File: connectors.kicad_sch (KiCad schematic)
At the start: 4 parts, among them J1 Conn_01x04_Pin, J2 Conn_01x04_Pin, J3 Conn_01x09_Pin, J4 Conn_02x03_Odd_Even

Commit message: Completed symbol-footprint associations.
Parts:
- J1, J2: footprint (none) -> Connector_PinHeader_2.54mm:PinHeader_1x04_P2.54mm_Vertical
- J3: footprint (none) -> Connector_PinHeader_2.54mm:PinHeader_1x09_P2.54mm_Vertical
- J4: footprint (none) -> Connector_PinHeader_2.54mm:PinHeader_2x03_P2.54mm_Vertical
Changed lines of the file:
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@@
       (effects (font (size 1.27 1.27)))
     )
-    (property "Footprint" "" (at 134.62 114.3 0)
+    (property "Footprint" "Connector_PinHeader_2.54mm:PinHeader_2x03_P2.54mm_Vertical" (at 134.62 114.3 0)
       (effects (font (size 1.27 1.27)) hide)
     )
@@
       (effects (font (size 1.27 1.27)))
     )
-    (property "Footprint" "" (at 107.95 87.63 0)
+    (property "Footprint" "Connector_PinHeader_2.54mm:PinHeader_1x04_P2.54mm_Vertical" (at 107.95 87.63 0)
       (effects (font (size 1.27 1.27)) hide)
     )
@@
       (effects (font (size 1.27 1.27)))
     )
-    (property "Footprint" "" (at 106.68 120.65 0)
+    (property "Footprint" "Connector_PinHeader_2.54mm:PinHeader_1x09_P2.54mm_Vertical" (at 106.68 120.65 0)
       (effects (font (size 1.27 1.27)) hide)
     )
@@
       (effects (font (size 1.27 1.27)))
     )
-    (property "Footprint" "" (at 135.89 87.63 0)
+    (property "Footprint" "Connector_PinHeader_2.54mm:PinHeader_1x04_P2.54mm_Vertical" (at 135.89 87.63 0)
       (effects (font (size 1.27 1.27)) hide)
     )

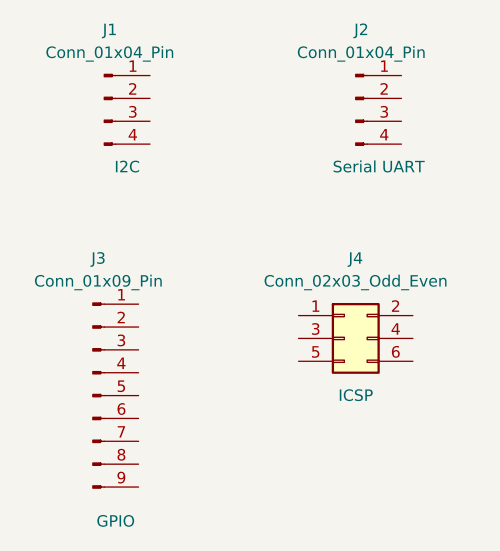
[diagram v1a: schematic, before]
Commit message: Completed wiring in second sheet.
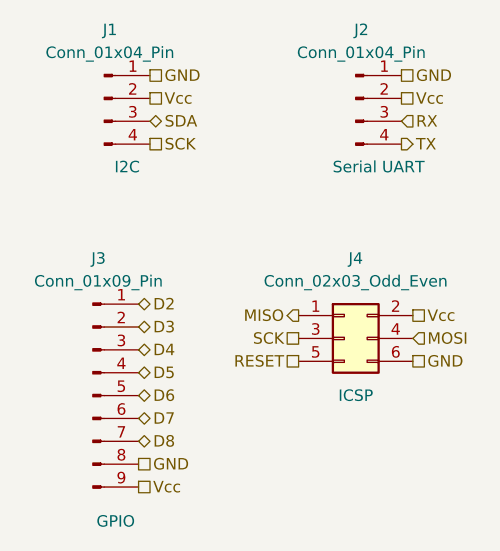
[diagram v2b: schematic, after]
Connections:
- net MISO: now reaches J4.1 (Pin_1)
- net Vcc: now reaches J4.2 (Pin_2)
- net Vcc: now also J1.2 (Pin_2), J2.2 (Pin_2), J3.9 (Pin_9)
- net SCK: now reaches J4.3 (Pin_3)
- net SCK: now also J1.4 (Pin_4)
- net MOSI: now reaches J4.4 (Pin_4)
- net RESET: now reaches J4.5 (Pin_5)
- net GND: now reaches J4.6 (Pin_6)
- net GND: now also J1.1 (Pin_1), J2.1 (Pin_1), J3.8 (Pin_8)
- net SDA: now reaches J1.3 (Pin_3)
- net D2: now reaches J3.1 (Pin_1)
- net D3: now reaches J3.2 (Pin_2)
- net D4: now reaches J3.3 (Pin_3)
- net D5: now reaches J3.4 (Pin_4)
- net D6: now reaches J3.5 (Pin_5)
- net D7: now reaches J3.6 (Pin_6)
- net D8: now reaches J3.7 (Pin_7)
- net RX: now reaches J2.3 (Pin_3)
- net TX: now reaches J2.4 (Pin_4)
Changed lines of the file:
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@@
 (kicad_sch (version 20230121) (generator eeschema)
   (paper "A4")
+  (hierarchical_label "MOSI" (shape input) (at 142.24 114.3 0) (fields_autoplaced)
+    (effects (font (size 1.27 1.27)) (justify left))
+  )
+  (hierarchical_label "Vcc" (shape passive) (at 113.03 87.63 0) (fields_autoplaced)
+    (effects (font (size 1.27 1.27)) (justify left))
+  )
+  (hierarchical_label "GND" (shape passive) (at 142.24 116.84 0) (fields_autoplaced)
+    (effects (font (size 1.27 1.27)) (justify left))
+  )
+  (hierarchical_label "D6" (shape bidirectional) (at 111.76 120.65 0) (fields_autoplaced)
+    (effects (font (size 1.27 1.27)) (justify left))
+  )
+  (hierarchical_label "RESET" (shape passive) (at 129.54 116.84 180) (fields_autoplaced)
+    (effects (font (size 1.27 1.27)) (justify right))
+  )
+  (hierarchical_label "GND" (shape passive) (at 140.97 85.09 0) (fields_autoplaced)
+    (effects (font (size 1.27 1.27)) (justify left))
+  )
+  (hierarchical_label "GND" (shape passive) (at 113.03 85.09 0) (fields_autoplaced)
+    (effects (font (size 1.27 1.27)) (justify left))
+  )
+  (hierarchical_label "Vcc" (shape passive) (at 111.76 130.81 0) (fields_autoplaced)
+    (effects (font (size 1.27 1.27)) (justify left))
+  )
+  (hierarchical_label "D3" (shape bidirectional) (at 111.76 113.03 0) (fields_autoplaced)
+    (effects (font (size 1.27 1.27)) (justify left))
+  )
+  (hierarchical_label "Vcc" (shape passive) (at 140.97 87.63 0) (fields_autoplaced)
+    (effects (font (size 1.27 1.27)) (justify left))
+  )
+  (hierarchical_label "D5" (shape bidirectional) (at 111.76 118.11 0) (fields_autoplaced)
+    (effects (font (size 1.27 1.27)) (justify left))
+  )
+  (hierarchical_label "D8" (shape bidirectional) (at 111.76 125.73 0) (fields_autoplaced)
+    (effects (font (size 1.27 1.27)) (justify left))
+  )
+  (hierarchical_label "SCK" (shape passive) (at 129.54 114.3 180) (fields_autoplaced)
+    (effects (font (size 1.27 1.27)) (justify right))
+  )
+  (hierarchical_label "SDA" (shape bidirectional) (at 113.03 90.17 0) (fields_autoplaced)
+    (effects (font (size 1.27 1.27)) (justify left))
+  )
+  (hierarchical_label "RX" (shape input) (at 140.97 90.17 0) (fields_autoplaced)
+    (effects (font (size 1.27 1.27)) (justify left))
+  )
+  (hierarchical_label "Vcc" (shape passive) (at 142.24 111.76 0) (fields_autoplaced)
+    (effects (font (size 1.27 1.27)) (justify left))
+  )
+  (hierarchical_label "D2" (shape bidirectional) (at 111.76 110.49 0) (fields_autoplaced)
+    (effects (font (size 1.27 1.27)) (justify left))
+  )
+  (hierarchical_label "MISO" (shape output) (at 129.54 111.76 180) (fields_autoplaced)
+    (effects (font (size 1.27 1.27)) (justify right))
+  )
+  (hierarchical_label "TX" (shape output) (at 140.97 92.71 0) (fields_autoplaced)
+    (effects (font (size 1.27 1.27)) (justify left))
+  )
+  (hierarchical_label "SCK" (shape passive) (at 113.03 92.71 0) (fields_autoplaced)
+    (effects (font (size 1.27 1.27)) (justify left))
+  )
+  (hierarchical_label "D4" (shape bidirectional) (at 111.76 115.57 0) (fields_autoplaced)
+    (effects (font (size 1.27 1.27)) (justify left))
+  )
+  (hierarchical_label "D7" (shape bidirectional) (at 111.76 123.19 0) (fields_autoplaced)
+    (effects (font (size 1.27 1.27)) (justify left))
+  )
+  (hierarchical_label "GND" (shape passive) (at 111.76 128.27 0) (fields_autoplaced)
+    (effects (font (size 1.27 1.27)) (justify left))
+  )
   (symbol (lib_id "Connector_Generic:Conn_02x03_Odd_Even") (at 134.62 114.3 0) (unit 1)
     (in_bom yes) (on_board yes) (dnp no)

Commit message: Fixed two defects in the schematic.
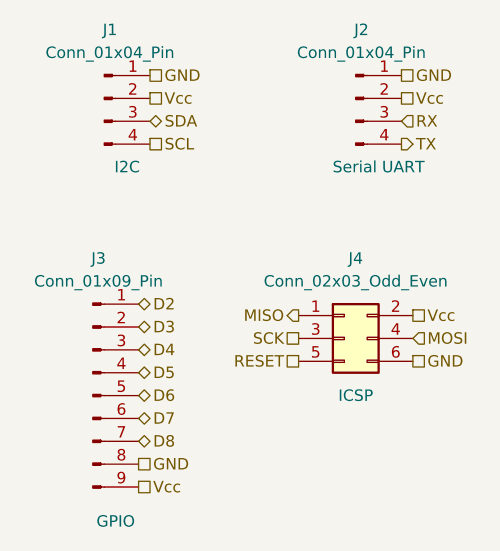
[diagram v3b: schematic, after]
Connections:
- net SCK: no longer J1.4 (Pin_4)
- new net SCL: J1.4 (Pin_4)
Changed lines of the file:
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@@
     (effects (font (size 1.27 1.27)) (justify left))
   )
-  (hierarchical_label "SCK" (shape passive) (at 113.03 92.71 0) (fields_autoplaced)
+  (hierarchical_label "SCL" (shape passive) (at 113.03 92.71 0) (fields_autoplaced)
     (effects (font (size 1.27 1.27)) (justify left))
   )
